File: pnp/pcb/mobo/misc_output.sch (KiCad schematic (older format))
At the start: 37 parts, among them J10 MF3, J11 MF4, J12 DOWNWARDS_LIGHT, J13 UPWARDS_LIGHT, J14 5V_INJECTION, J15 RS-485_1, J16 RS-485_2, J17 RS-485_3, J21 I2C, J22 SPI, J23 AUX1, J24 AUX2, J6 SERVO1, J7 SERVO2, J8 MF1, J9 MF2, Q1 IRF540N, Q2 IRF540N, Q3 IRF540N, Q4 IRF540N, U2 SP3485EN, U3 SP3485EN, U4 SP3485EN

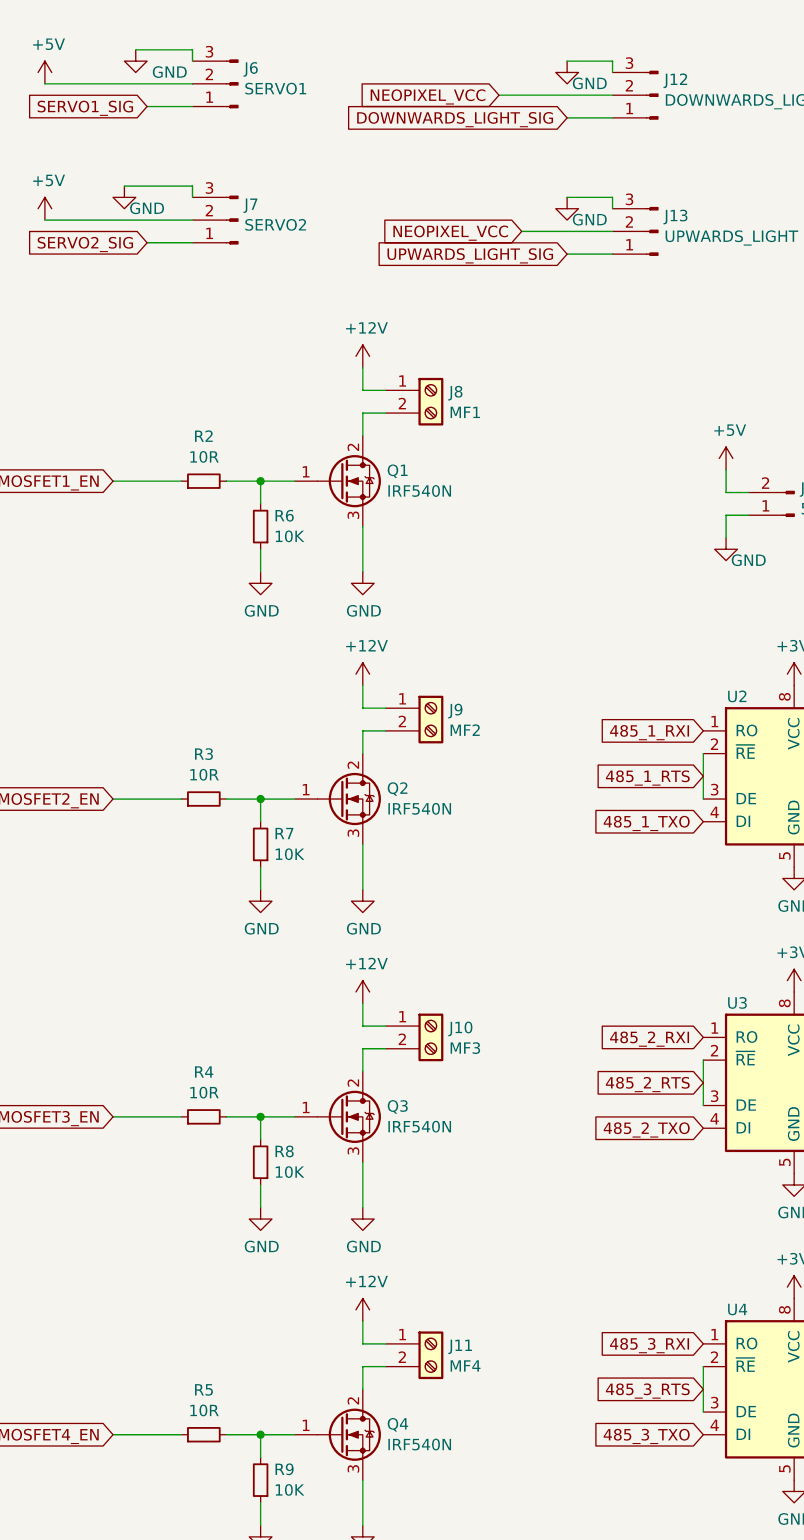
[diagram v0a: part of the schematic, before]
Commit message: first chunk of routing. most power stuff is done, plus some misc crystals and such. gpio is the big chunk left
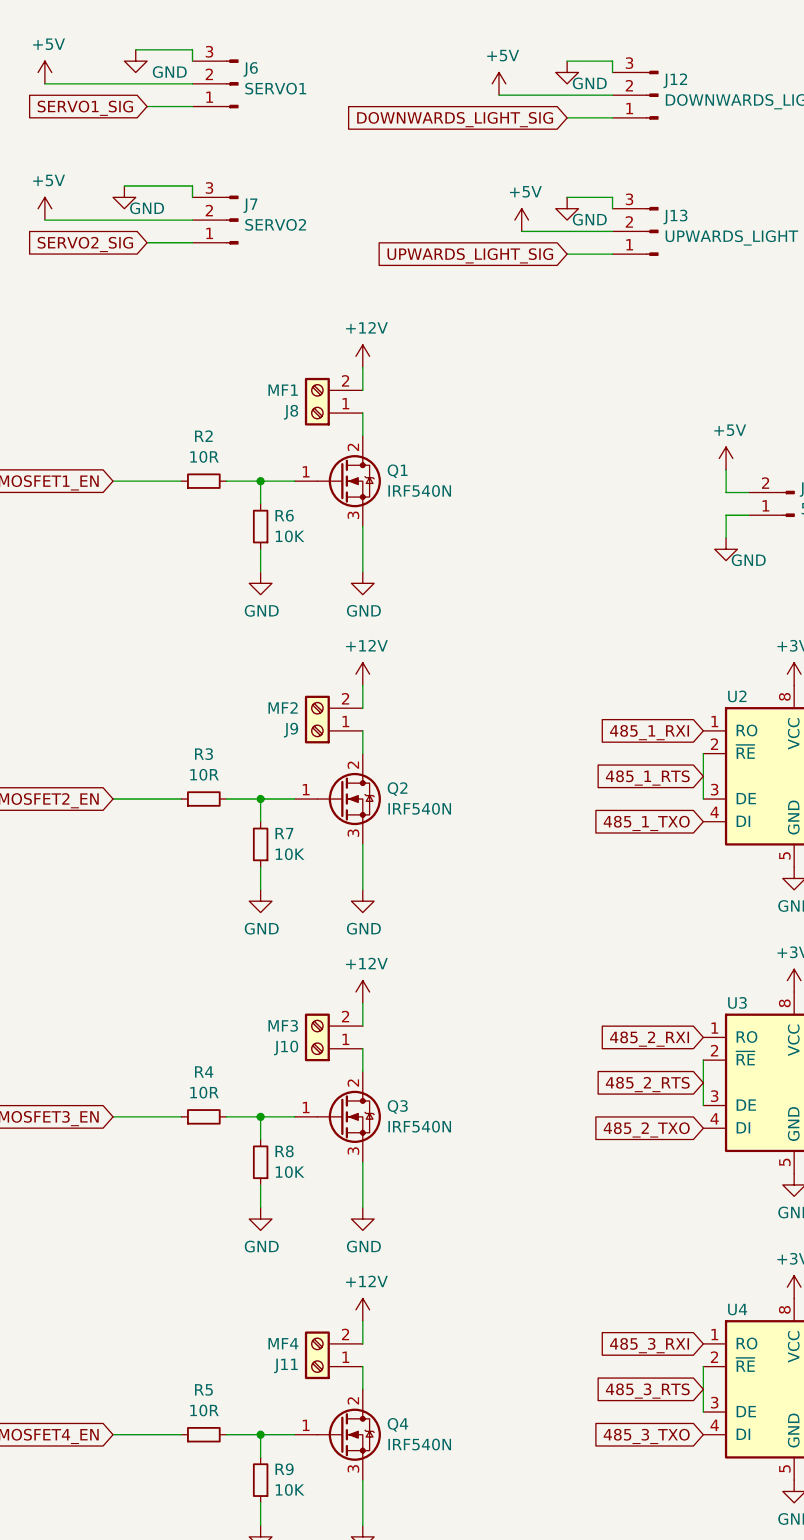
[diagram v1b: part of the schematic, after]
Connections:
- net labels removed: NEOPIXEL_VCC
- wire segments 122 -> 114
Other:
- moved on the sheet: J10, J11, J8, J9
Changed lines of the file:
@@
 L Connector:Screw_Terminal_01x02 J8
 U 1 1 5EBF7CF2
-P 2650 2250
-F 0 "J8" H 2730 2242 50  0000 L CNN
-F 1 "MF1" H 2730 2151 50  0000 L CNN
-F 2 "Connector_JST:JST_XH_B2B-XH-A_1x02_P2.50mm_Vertical" H 2650 2250 50  0001 C CNN
-F 3 "~" H 2650 2250 50  0001 C CNN
-	1    2650 2250
-	1    0    0    -1
+P 2150 2350
+F 0 "J8" H 2230 2342 50  0000 L CNN
+F 1 "MF1" H 2230 2251 50  0000 L CNN
+F 2 "Connector_JST:JST_XH_B2B-XH-A_1x02_P2.50mm_Vertical" H 2150 2350 50  0001 C CNN
+F 3 "~" H 2150 2350 50  0001 C CNN
+	1    2150 2350
+	-1   0    0    1
 $EndComp
 $Comp
@@
 	1900 3050 1900 2950
 Wire Wire Line
-	2450 2350 2350 2350
-Wire Wire Line
 	2350 2350 2350 2450
-Wire Wire Line
-	2450 2250 2350 2250
 Wire Wire Line
 	2350 2250 2350 2150
@@
 L Connector:Screw_Terminal_01x02 J9
 U 1 1 5EC0DF73
-P 2650 3650
-F 0 "J9" H 2730 3642 50  0000 L CNN
-F 1 "MF2" H 2730 3551 50  0000 L CNN
-F 2 "Connector_JST:JST_XH_B2B-XH-A_1x02_P2.50mm_Vertical" H 2650 3650 50  0001 C CNN
-F 3 "~" H 2650 3650 50  0001 C CNN
-	1    2650 3650
-	1    0    0    -1
+P 2150 3750
+F 0 "J9" H 2230 3742 50  0000 L CNN
+F 1 "MF2" H 2230 3651 50  0000 L CNN
+F 2 "Connector_JST:JST_XH_B2B-XH-A_1x02_P2.50mm_Vertical" H 2150 3750 50  0001 C CNN
+F 3 "~" H 2150 3750 50  0001 C CNN
+	1    2150 3750
+	-1   0    0    1
 $EndComp
 $Comp
@@
 	1900 4450 1900 4350
 Wire Wire Line
-	2450 3750 2350 3750
-Wire Wire Line
 	2350 3750 2350 3850
-Wire Wire Line
-	2450 3650 2350 3650
 Wire Wire Line
 	2350 3650 2350 3550
@@
 L Connector:Screw_Terminal_01x02 J10
 U 1 1 5EC13985
-P 2650 5050
-F 0 "J10" H 2730 5042 50  0000 L CNN
-F 1 "MF3" H 2730 4951 50  0000 L CNN
-F 2 "Connector_JST:JST_XH_B2B-XH-A_1x02_P2.50mm_Vertical" H 2650 5050 50  0001 C CNN
-F 3 "~" H 2650 5050 50  0001 C CNN
-	1    2650 5050
-	1    0    0    -1
+P 2150 5150
+F 0 "J10" H 2230 5142 50  0000 L CNN
+F 1 "MF3" H 2230 5051 50  0000 L CNN
+F 2 "Connector_JST:JST_XH_B2B-XH-A_1x02_P2.50mm_Vertical" H 2150 5150 50  0001 C CNN
+F 3 "~" H 2150 5150 50  0001 C CNN
+	1    2150 5150
+	-1   0    0    1
 $EndComp
 $Comp
@@
 	1900 5850 1900 5750
 Wire Wire Line
-	2450 5150 2350 5150
-Wire Wire Line
 	2350 5150 2350 5250
-Wire Wire Line
-	2450 5050 2350 5050
 Wire Wire Line
 	2350 5050 2350 4950
@@
 L Connector:Screw_Terminal_01x02 J11
 U 1 1 5EC17A77
-P 2650 6450
-F 0 "J11" H 2730 6442 50  0000 L CNN
-F 1 "MF4" H 2730 6351 50  0000 L CNN
-F 2 "Connector_JST:JST_XH_B2B-XH-A_1x02_P2.50mm_Vertical" H 2650 6450 50  0001 C CNN
-F 3 "~" H 2650 6450 50  0001 C CNN
-	1    2650 6450
-	1    0    0    -1
+P 2150 6550
+F 0 "J11" H 2230 6542 50  0000 L CNN
+F 1 "MF4" H 2230 6451 50  0000 L CNN
+F 2 "Connector_JST:JST_XH_B2B-XH-A_1x02_P2.50mm_Vertical" H 2150 6550 50  0001 C CNN
+F 3 "~" H 2150 6550 50  0001 C CNN
+	1    2150 6550
+	-1   0    0    1
 $EndComp
 $Comp
@@
 	1900 7250 1900 7150
 Wire Wire Line
-	2450 6550 2350 6550
-Wire Wire Line
 	2350 6550 2350 6650
-Wire Wire Line
-	2450 6450 2350 6450
 Wire Wire Line
 	2350 6450 2350 6350
@@
 	1    0    0    -1
 $EndComp
-Text GLabel 3050 1550 0    50   Input ~ 0
-NEOPIXEL_VCC
-Text GLabel 2950 950  0    50   Input ~ 0
-NEOPIXEL_VCC
 $Comp
 L Interface_UART:SP3485EN U3
@@
 Text GLabel 5800 2400 0    50   Input ~ 0
 SCK
+$Comp
+L power:+5V #PWR0210
+U 1 1 5F1781C2
+P 2950 950
+F 0 "#PWR0210" H 2950 800 50  0001 C CNN
+F 1 "+5V" H 2965 1123 50  0000 C CNN
+F 2 "" H 2950 950 50  0001 C CNN
+F 3 "" H 2950 950 50  0001 C CNN
+	1    2950 950
+	1    0    0    -1
+$EndComp
+$Comp
+L power:+5V #PWR0211
+U 1 1 5F17BF64
+P 3050 1550
+F 0 "#PWR0211" H 3050 1400 50  0001 C CNN
+F 1 "+5V" H 3065 1723 50  0000 C CNN
+F 2 "" H 3050 1550 50  0001 C CNN
+F 3 "" H 3050 1550 50  0001 C CNN
+	1    3050 1550
+	1    0    0    -1
+$EndComp
 $EndSCHEMATC

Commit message: switched to more monolithic vacuum sensor. rerouted for it. routed aux ports. exported and ordered. this commit exactly reflects REV001 hardware.
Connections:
- net labels added: AUX1-A1, AUX1-A2, AUX1-D1, AUX1-D2, AUX2-A1, AUX2-A2, AUX2-D1, AUX2-D2
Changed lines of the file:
@@
 	1    0    0    -1
 $EndComp
+Text GLabel 8150 1250 0    50   Input ~ 0
+AUX1-D1
+Text GLabel 8150 1350 0    50   Input ~ 0
+AUX1-D2
+Text GLabel 8150 2500 0    50   Input ~ 0
+AUX2-D1
+Text GLabel 8150 2600 0    50   Input ~ 0
+AUX2-D2
+Text GLabel 8150 1550 0    50   Input ~ 0
+AUX1-A2
+Text GLabel 8150 2800 0    50   Input ~ 0
+AUX2-A2
+Text GLabel 8150 1450 0    50   Input ~ 0
+AUX1-A1
+Text GLabel 8150 2700 0    50   Input ~ 0
+AUX2-A1
 $EndSCHEMATC

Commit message: improved main sch layout a bit, updated fet footprint to TO-252-2
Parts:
- Q1, Q2, Q3, Q4: footprint Package_TO_SOT_SMD:TO-263-3_TabPin2 -> Package_TO_SOT_SMD:TO-252-2
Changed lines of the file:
@@
 F 0 "Q1" H 2456 2696 50  0000 L CNN
 F 1 "IRF540N" H 2456 2605 50  0000 L CNN
-F 2 "Package_TO_SOT_SMD:TO-263-3_TabPin2" H 2500 2575 50  0001 L CIN
+F 2 "Package_TO_SOT_SMD:TO-252-2" H 2500 2575 50  0001 L CIN
 F 3 "http://www.irf.com/product-info/datasheets/data/irf540n.pdf" H 2250 2650 50  0001 L CNN
 	1    2250 2650
@@
 F 0 "Q2" H 2456 4096 50  0000 L CNN
 F 1 "IRF540N" H 2456 4005 50  0000 L CNN
-F 2 "Package_TO_SOT_SMD:TO-263-3_TabPin2" H 2500 3975 50  0001 L CIN
+F 2 "Package_TO_SOT_SMD:TO-252-2" H 2500 3975 50  0001 L CIN
 F 3 "http://www.irf.com/product-info/datasheets/data/irf540n.pdf" H 2250 4050 50  0001 L CNN
 	1    2250 4050
@@
 F 0 "Q3" H 2456 5496 50  0000 L CNN
 F 1 "IRF540N" H 2456 5405 50  0000 L CNN
-F 2 "Package_TO_SOT_SMD:TO-263-3_TabPin2" H 2500 5375 50  0001 L CIN
+F 2 "Package_TO_SOT_SMD:TO-252-2" H 2500 5375 50  0001 L CIN
 F 3 "http://www.irf.com/product-info/datasheets/data/irf540n.pdf" H 2250 5450 50  0001 L CNN
 	1    2250 5450
@@
 F 0 "Q4" H 2456 6896 50  0000 L CNN
 F 1 "IRF540N" H 2456 6805 50  0000 L CNN
-F 2 "Package_TO_SOT_SMD:TO-263-3_TabPin2" H 2500 6775 50  0001 L CIN
+F 2 "Package_TO_SOT_SMD:TO-252-2" H 2500 6775 50  0001 L CIN
 F 3 "http://www.irf.com/product-info/datasheets/data/irf540n.pdf" H 2250 6850 50  0001 L CNN
 	1    2250 6850

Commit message: switched to two 10-pin aux ports
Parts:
- removed J21: I2C, Connector_JST:JST_XH_B4B-XH-A_1x04_P2.50mm_Vertical, symbol Connector:Conn_01x04_Female
- removed J22: SPI, Connector_JST:JST_XH_B5B-XH-A_1x05_P2.50mm_Vertical, symbol Connector:Conn_01x05_Female
- removed J23: AUX1, Connector_JST:JST_XH_B6B-XH-A_1x06_P2.50mm_Vertical, symbol Connector:Conn_01x06_Female
- removed J24: AUX2, Connector_JST:JST_XH_B6B-XH-A_1x06_P2.50mm_Vertical, symbol Connector:Conn_01x06_Female
- added J?: AUX1, symbol Connector:Conn_01x10_Male
- added J?: AUX2, symbol Connector:Conn_01x10_Male
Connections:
- net labels added: MISO, MOSI
- net labels removed: AUX1-D2, AUX2-D2, CIPO, COPI
- wire segments 114 -> 122
